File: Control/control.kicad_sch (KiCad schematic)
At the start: 13 parts, among them J2-J1 Conn_01x10, J3-J1 Conn_01x10, U1 TLV2372, U2 ACS71240KEXBLT-050U5, U3 ACS71240KEXBLT-010B3

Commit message: mostly done with first order layout
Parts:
- added C_{smooth}2: 4.7u, Capacitor_SMD:C_0805_2012Metric_Pad1.18x1.45mm_HandSolder, symbol Device:C
- added R_{sens,bottom}1, R_{sens,bottom}2: 2k, Resistor_SMD:R_0603_1608Metric_Pad0.98x0.95mm_HandSolder, symbol Device:R_Small_US
- added R_{sens,top}1, R_{sens,top}2: 16k, Resistor_SMD:R_0603_1608Metric_Pad0.98x0.95mm_HandSolder, symbol Device:R_Small_US
- added U2: TLV2372, Package_SO:SOIC-8_3.9x4.9mm_P1.27mm, symbol Amplifier_Operational:TLV2372
- renumbered C_{smooth}2 to C_{smooth}1, C_{smooth}1 to C_{smooth}3, C_{smooth}3 to C_{smooth}4, C_{smooth}4 to C_{smooth}5, U2 to U3, U3 to U4
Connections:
- net +3V3: now also C_{smooth}2.1, U2.8 (V+)
- net GND: now also C_{smooth}2.2, R_{sens,bottom}1.1, U2.4 (V-)
- net I_{bat,out+}: now also R_{sens,top}1.1
- net Vout renamed V_{sc,sens}
- new net: R_{sens,bottom}2.1, R_{sens,top}1.2, U2.3 (+)
- new net: R_{sens,bottom}1.2, R_{sens,top}2.2, U2.2 (-)
- new net GNDPWR: R_{sens,top}2.1
- new net V_{bat,sens}: R_{sens,bottom}2.2, U2.1
- no-connect marks 11 -> 14
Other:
- note added: "Battery Voltage Sensing"
- note added: "Differential Amplifier V_{out}= (V_{cap-}-V_{cap+}) ~{ 8 }"
- company: (none) -> UT Robomaster
- title: (none) -> Controls and Sensing Board
- moved on the sheet: C_{smooth}1, C_{smooth}3, C_{smooth}4, C_{smooth}5, J2-J1, J3-J1, R1, R2, R3, R4, U1A, U1B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

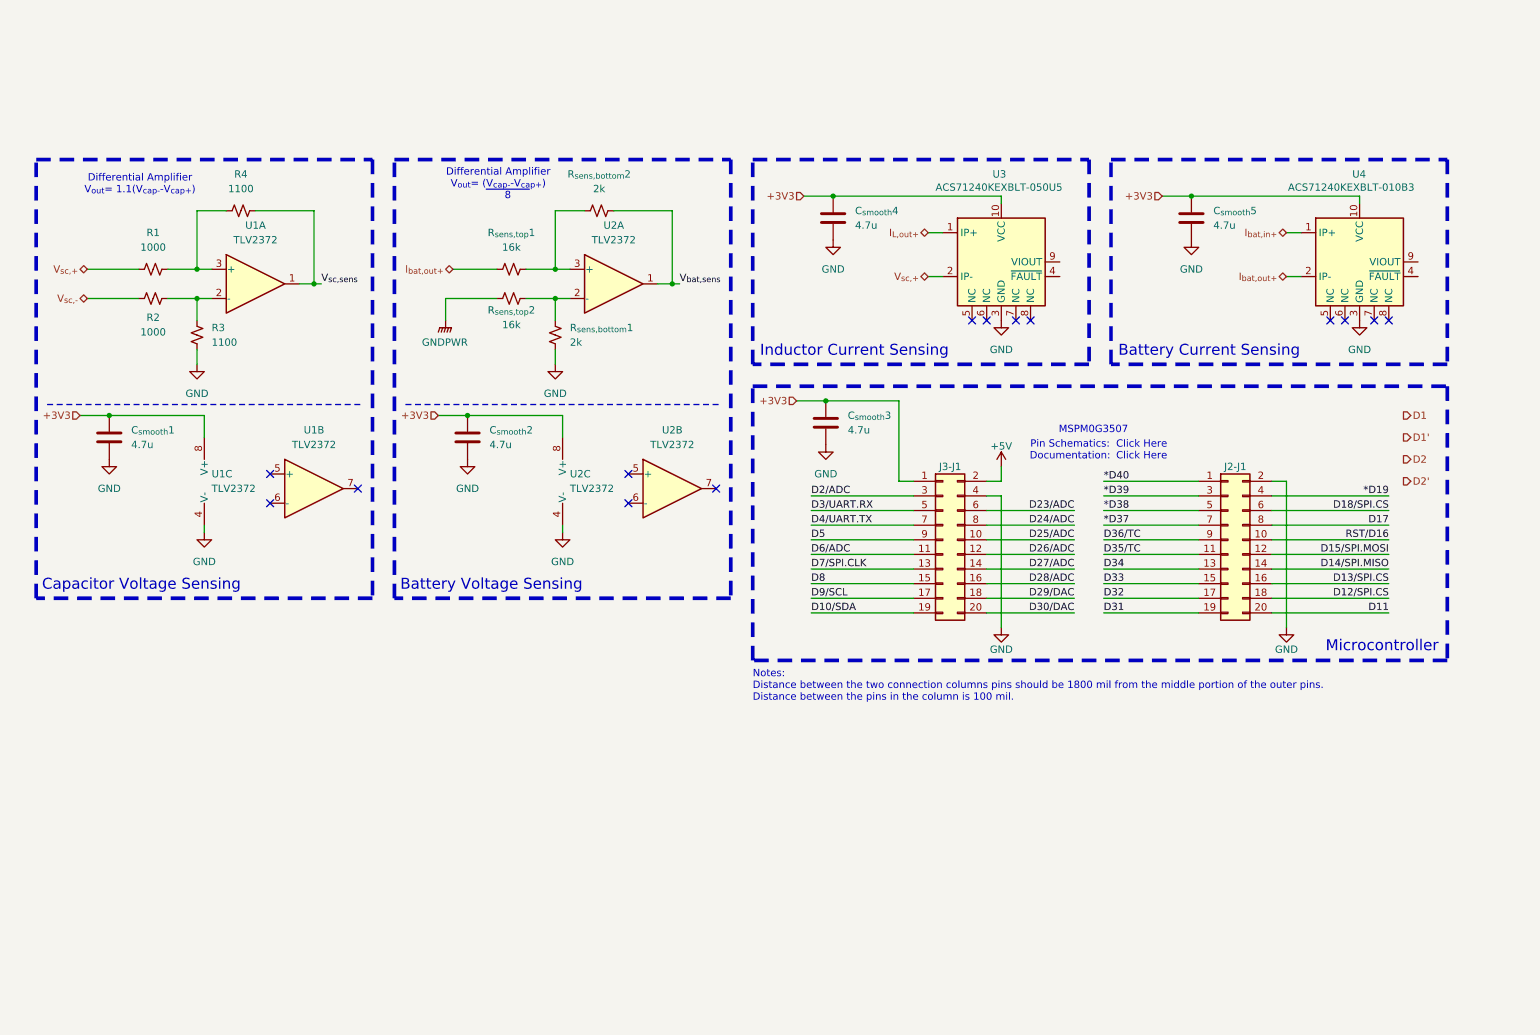
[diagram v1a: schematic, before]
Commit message: I FINALLY FIGURED OUT THE CONTROL SCHEME I NEEDED A SQUARE ROOT
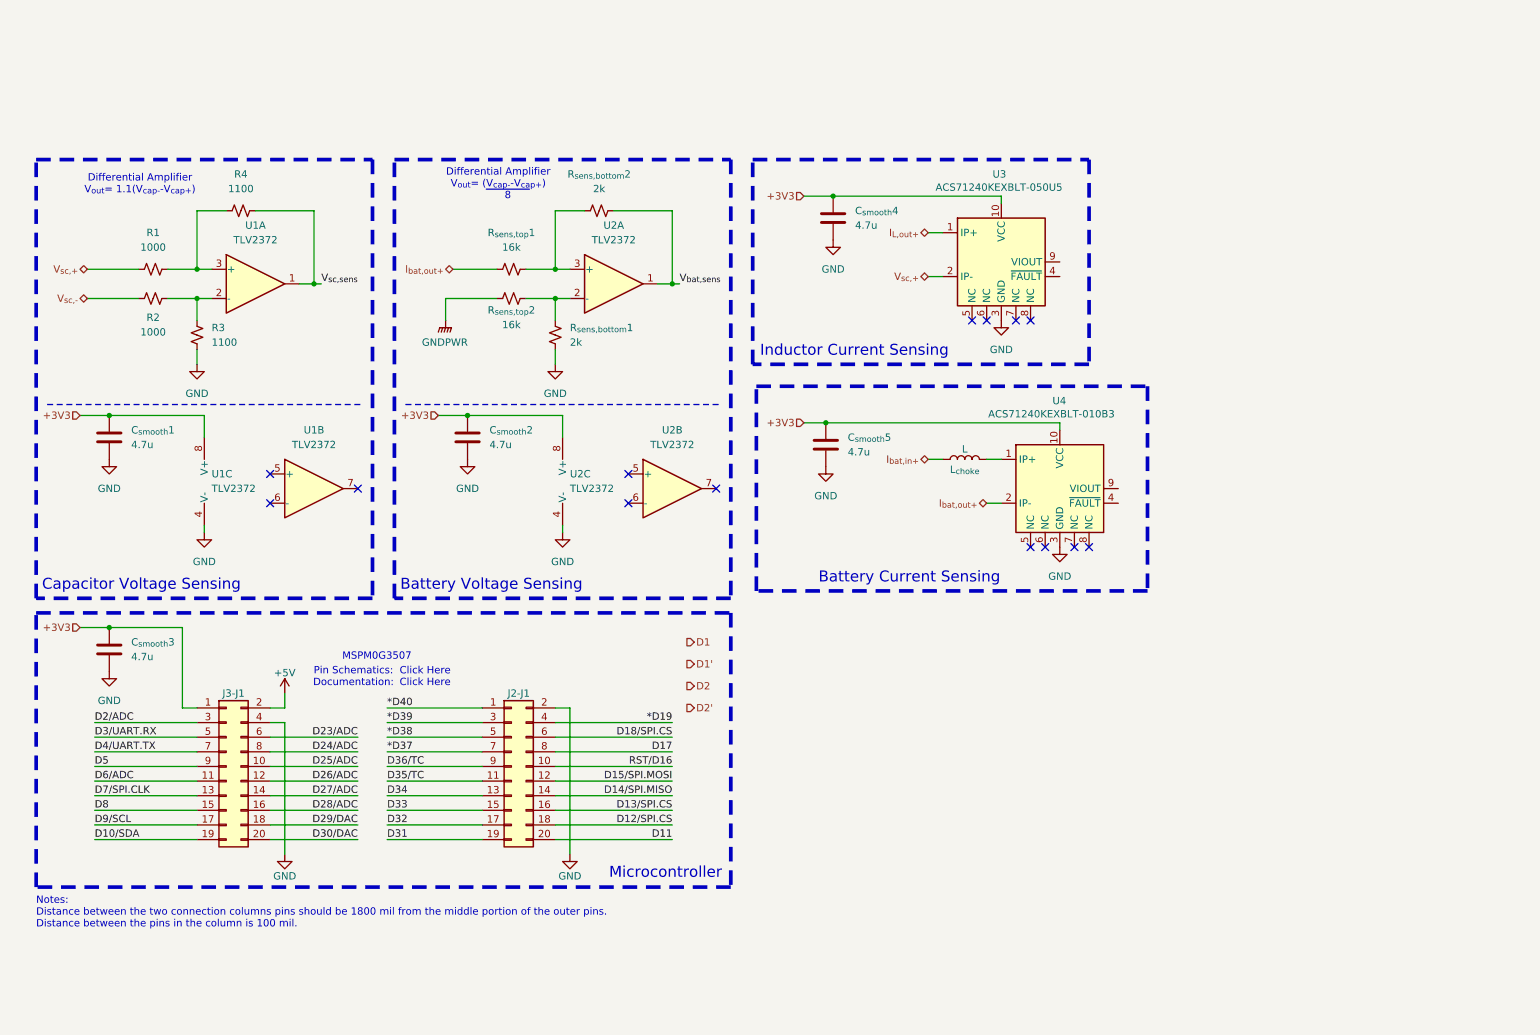
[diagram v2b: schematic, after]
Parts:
- added L_{choke}: L, symbol Device:L
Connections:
- net I_{bat,in+}: now also L_{choke}.1; no longer U4.1 (IP+)
- new net: L_{choke}.2, U4.1 (IP+)
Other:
- moved on the sheet: C_{smooth}3, C_{smooth}5, J2-J1, J3-J1, U4

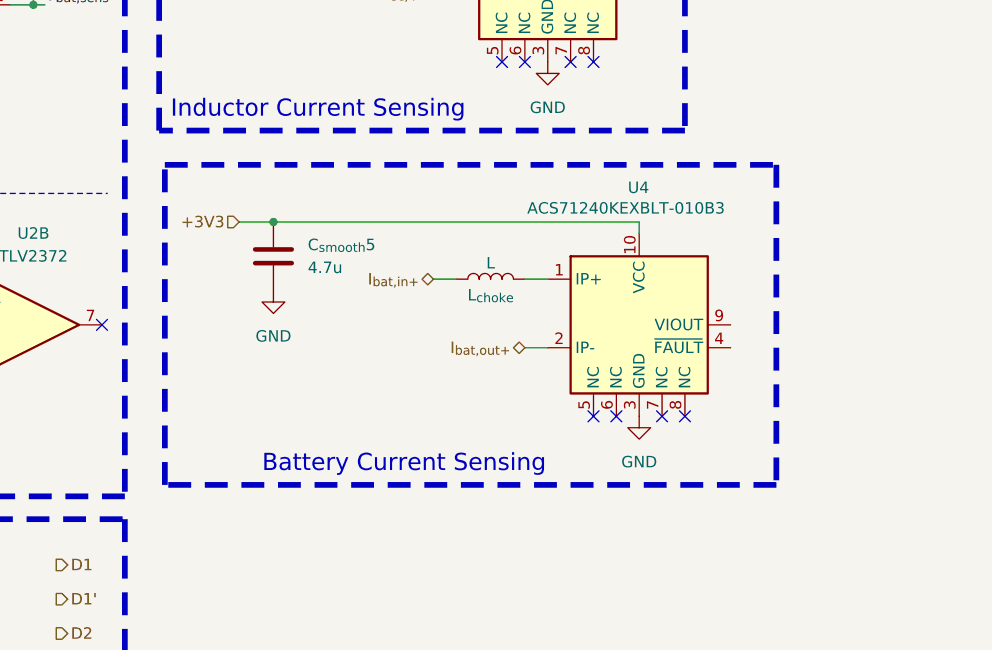
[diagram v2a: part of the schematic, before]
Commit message: critical loops trace
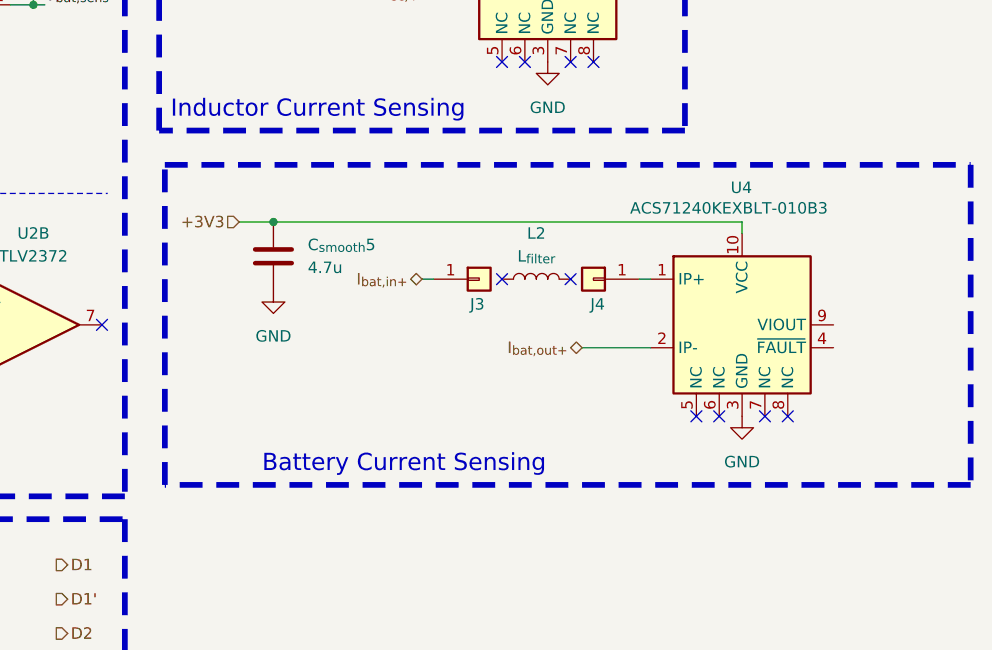
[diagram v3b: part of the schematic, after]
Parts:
- removed L_{choke}: L, symbol Device:L
- added J3, J4: Conn_01x01, Robomaster_Passives:Inductor_wire_conn, symbol Connector_Generic:Conn_01x01
- added L2: L_{filter}, symbol Device:L
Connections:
- net I_{bat,in+}: now also J3.1 (Pin_1)
- net at U4.1 (IP+): now also J4.1 (Pin_1)
- no-connect marks 14 -> 16
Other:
- moved on the sheet: U4

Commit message: ok hopefully this doesnt break everything, committing after doing in kicadlib submod
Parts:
- added C_{smooth}8: 4.7u, Capacitor_SMD:C_0805_2012Metric_Pad1.18x1.45mm_HandSolder, symbol Device:C
- added U5: ACS71240KEXBLT-010B3, Sensor_Current:Allegro_QFN-12-10-1EP_3x3mm_P0.5mm, symbol Sensor_Current:ACS711xEXLT-15AB
- added U6: LP-MSPM0G3507, MSPM0:ti_LP_MSPM0G3507, symbol ECE319K:LP-MSPM0G3507
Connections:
- net +3V3: now also C_{smooth}8.1, U5.10 (VCC)
- net GND: now also C_{smooth}8.2, U5.3 (GND)
- new net I_{out sense+}: U5.1 (IP+)
- new net I_{out sense-}: U5.2 (IP-)
- no-connect marks 16 -> 20

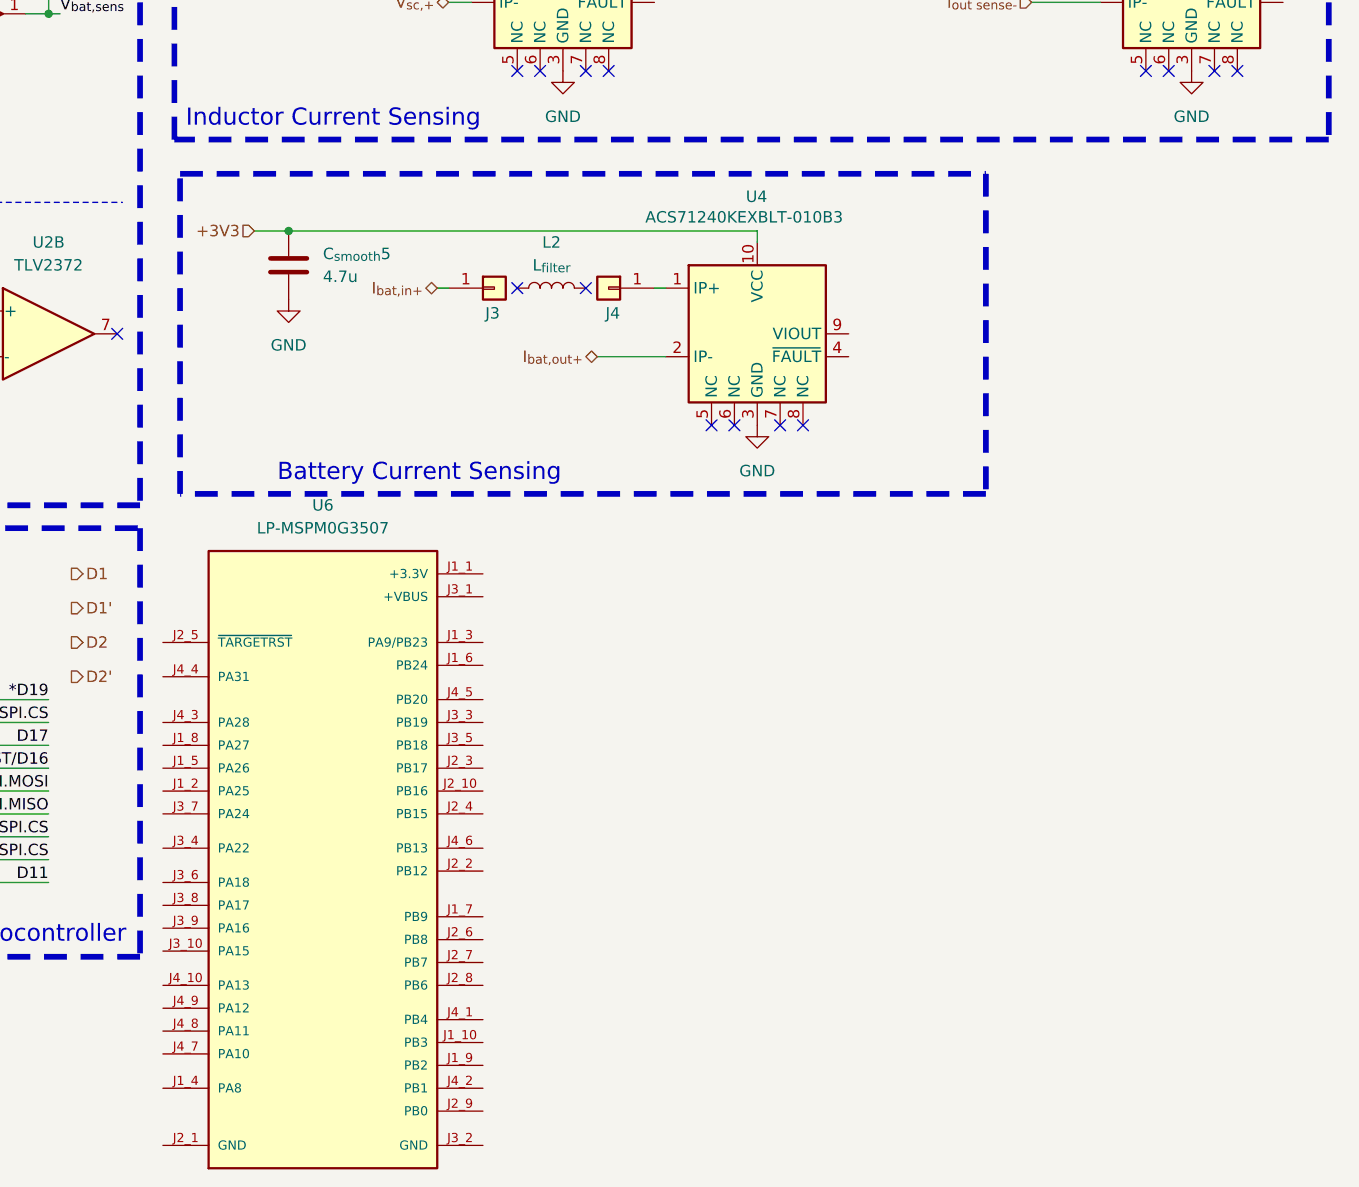
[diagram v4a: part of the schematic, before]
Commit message: added mspm0 fp, still need to map pin nets on sym in schematic, in process of doing redesign to min power path
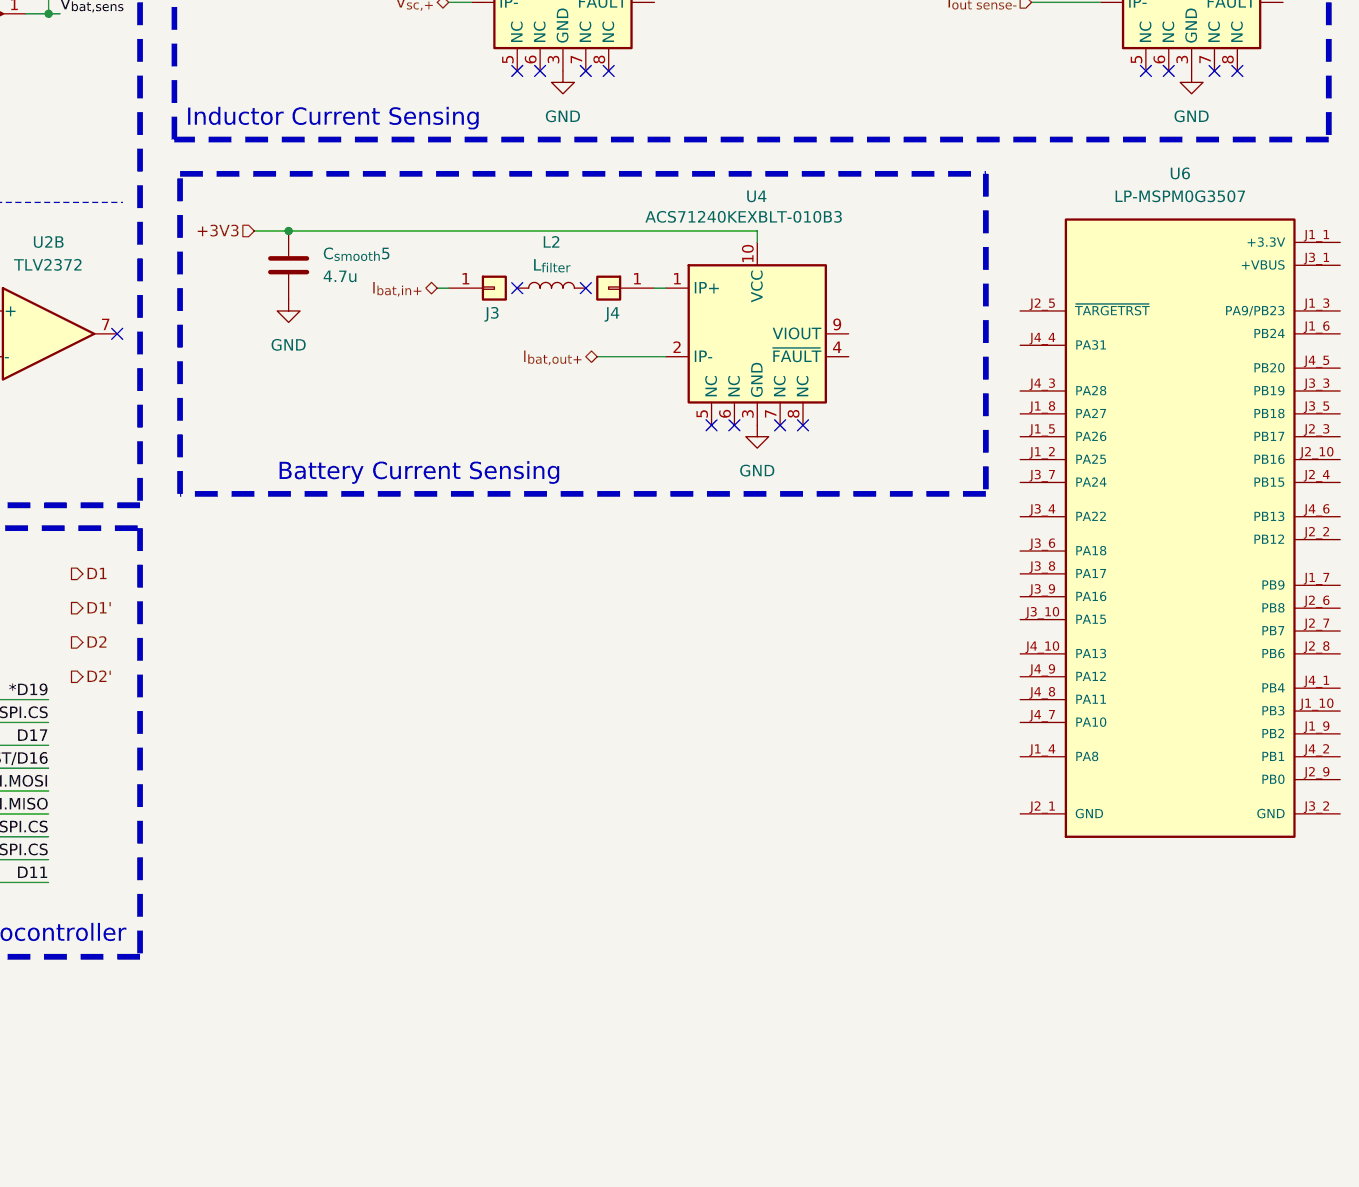
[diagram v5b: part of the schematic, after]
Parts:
- U6: now left out of the parts list
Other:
- moved on the sheet: U6
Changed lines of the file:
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@@
 	(symbol
 		(lib_id "ECE319K:LP-MSPM0G3507")
-		(at 163.83 166.37 0)
+		(at 259.08 129.54 0)
 		(unit 1)
 		(exclude_from_sim no)
-		(in_bom yes)
+		(in_bom no)
 		(on_board yes)
 		(dnp no)
 		(fields_autoplaced yes)
 		(property "Reference" "U6"
-			(at 163.83 128.27 0)
+			(at 259.08 91.44 0)
 			(effects
 				(font
@@
 		)
 		(property "Value" "LP-MSPM0G3507"
-			(at 163.83 130.81 0)
+			(at 259.08 93.98 0)
 			(effects
 				(font
@@
 		)
 		(property "Footprint" "MSPM0:ti_LP_MSPM0G3507"
-			(at 163.83 165.1 0)
+			(at 259.08 128.27 0)
 			(effects
 				(font
@@
 		)
 		(property "Datasheet" "https://www.ti.com/tool/LP-MSPM0G3507"
-			(at 171.45 130.81 0)
+			(at 266.7 93.98 0)
 			(effects
 				(font
@@
 		)
 		(property "Description" "LaunchPad"
-			(at 163.83 166.37 0)
+			(at 259.08 129.54 0)
 			(effects
 				(font
@@
 		)
 		(property "Distributor" "Mouser"
-			(at 163.83 163.83 0)
+			(at 259.08 127 0)
 			(effects
 				(font
@@
 		)
 		(property "Manufacturer" "Texas Instruments"
-			(at 163.83 163.83 0)
+			(at 259.08 127 0)
 			(effects
 				(font
@@
 		)
 		(property "P/N" "LP-MSPM0G3507"
-			(at 161.29 137.16 0)
+			(at 256.54 100.33 0)
 			(effects
 				(font
@@
 		)
 		(property "LCSC Part #" ""
-			(at 163.83 166.37 0)
+			(at 259.08 129.54 0)
 			(effects
 				(font
@@
 		)
 		(property "Cost" "22.60"
-			(at 163.83 163.83 0)
+			(at 259.08 127 0)
 			(effects
 				(font

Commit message: via stitching on fets, fixed sheet pin (not label on parent) for isense, messed around with design
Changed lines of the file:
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@@
 	)
 	(hierarchical_label "I_{out sense+}"
-		(shape input)
+		(shape bidirectional)
 		(at 242.57 64.77 180)
 		(effects
@@
 	)
 	(hierarchical_label "I_{out sense-}"
-		(shape input)
+		(shape bidirectional)
 		(at 242.57 72.39 180)
 		(effects
